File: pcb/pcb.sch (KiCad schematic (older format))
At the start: 20 parts, among them J1 BAT+, J2 BAT-, J3 Molex, SW1 Reset, SW2 Flash, U1 BOB-13263, U2 ESP-12F, U3 TP4056, U4 GY-521, U5 VREG

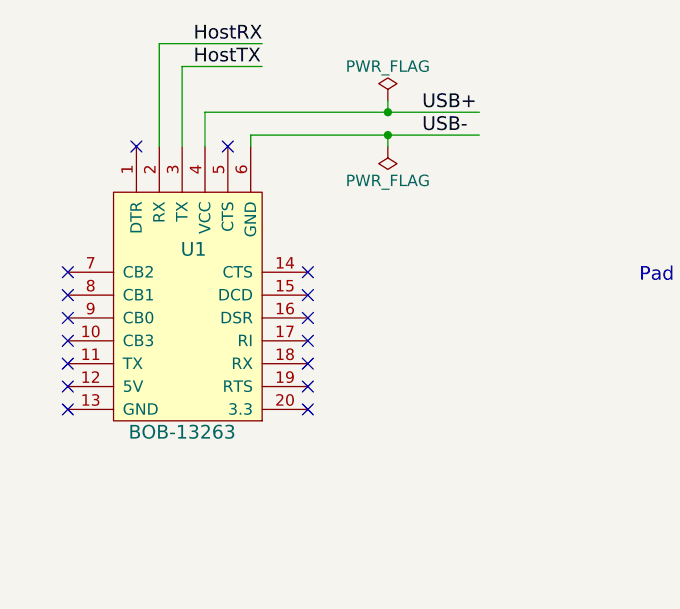
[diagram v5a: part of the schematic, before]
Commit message: PCB: use a smaller FTDI breakout board
The CP2102 USB Micro breakout boards look like they fit between the
pins of the TP4056 breakout board, which simplifies installation.
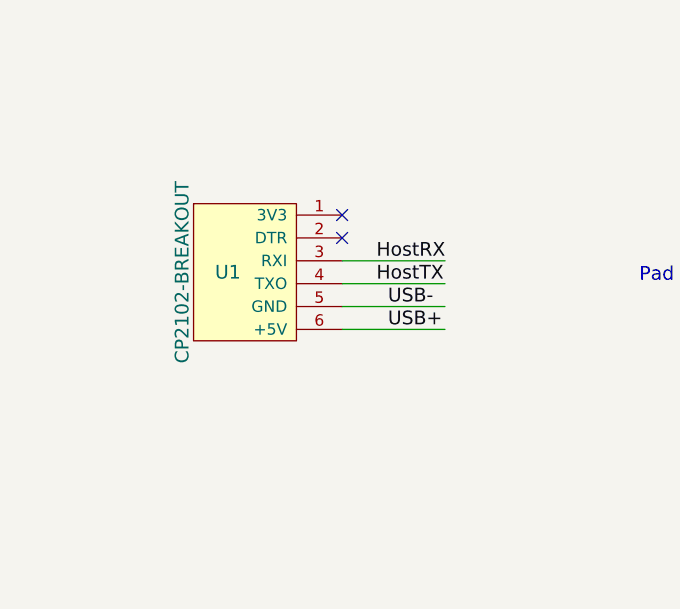
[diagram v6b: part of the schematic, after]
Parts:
- removed U1: BOB-13263, BOB13263:BOB-13263-TOP, symbol BOB-13263
- added U1: CP2102-BREAKOUT, CP2102-BRK:CP2102-BREAKOUT, symbol CP2102-BREAKOUT
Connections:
- wire segments 67 -> 61
- no-connect marks 28 -> 14
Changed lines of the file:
@@
 LIBS:tp4056
 LIBS:bob-13263
+LIBS:cp2102-breakout
 LIBS:pcb-cache
 EELAYER 25 0
@@
 $EndComp
 $Comp
-L PWR_FLAG #FLG01
-U 1 1 5B217D4E
-P 3800 1600
-F 0 "#FLG01" H 3800 1675 50  0001 C CNN
-F 1 "PWR_FLAG" H 3800 1750 50  0000 C CNN
-F 2 "" H 3800 1600 50  0001 C CNN
-F 3 "" H 3800 1600 50  0001 C CNN
-	1    3800 1600
-	1    0    0    -1
-$EndComp
-$Comp
-L PWR_FLAG #FLG02
-U 1 1 5B219669
-P 3800 1800
-F 0 "#FLG02" H 3800 1875 50  0001 C CNN
-F 1 "PWR_FLAG" H 3800 1950 50  0000 C CNN
-F 2 "" H 3800 1800 50  0001 C CNN
-F 3 "" H 3800 1800 50  0001 C CNN
-	1    3800 1800
-	-1   0    0    1
-$EndComp
-$Comp
 L SW_Push SW2
 U 1 1 5B21A301
@@
 	0    1    1    0
 $EndComp
-Text Label 3950 1650 0    60   ~ 0
+Text Label 3800 2600 0    60   ~ 0
 USB+
-Text Label 2950 1450 0    60   ~ 0
+Text Label 3750 2400 0    60   ~ 0
 HostTX
-Text Label 2950 1350 0    60   ~ 0
+Text Label 3750 2300 0    60   ~ 0
 HostRX
 Text Label 7300 2400 0    60   ~ 0
@@
 Text Label 5400 2150 1    60   ~ 0
 BAT+
-Text Label 3950 1750 0    60   ~ 0
+Text Label 3800 2500 0    60   ~ 0
 USB-
 Text Label 2300 5450 0    60   ~ 0
@@
 $EndComp
 $Comp
-L PWR_FLAG #FLG03
+L PWR_FLAG #FLG01
 U 1 1 5B22D046
 P 2850 5950
-F 0 "#FLG03" H 2850 6025 50  0001 C CNN
+F 0 "#FLG01" H 2850 6025 50  0001 C CNN
 F 1 "PWR_FLAG" H 2850 6100 50  0000 C CNN
 F 2 "" H 2850 5950 50  0001 C CNN
@@
 	-1   0    0    1
 $EndComp
-$Comp
-L BOB-13263 U1
-U 1 1 5B21DE34
-P 2600 2000
-F 0 "U1" H 2950 1750 60  0000 C CNN
-F 1 "BOB-13263" H 2900 950 60  0000 C CNN
-F 2 "BOB13263:BOB-13263-TOP" H 2600 2000 60  0001 C CNN
-F 3 "" H 2600 2000 60  0001 C CNN
-	1    2600 2000
-	1    0    0    -1
-$EndComp
-NoConn ~ 3100 1800
-NoConn ~ 2700 1800
-NoConn ~ 3450 2350
-NoConn ~ 3450 2450
-NoConn ~ 3450 2550
-NoConn ~ 3450 2650
-NoConn ~ 3450 2750
-NoConn ~ 3450 2850
-NoConn ~ 3450 2950
-NoConn ~ 2400 2950
-NoConn ~ 2400 2850
-NoConn ~ 2400 2750
-NoConn ~ 2400 2650
-NoConn ~ 2400 2550
-NoConn ~ 2400 2450
-NoConn ~ 2400 2350
-$Comp
-L PWR_FLAG #FLG04
+NoConn ~ 3600 2100
+NoConn ~ 3600 2200
+$Comp
+L PWR_FLAG #FLG02
 U 1 1 5B2225EE
 P 5700 3100
-F 0 "#FLG04" H 5700 3175 50  0001 C CNN
+F 0 "#FLG02" H 5700 3175 50  0001 C CNN
 F 1 "PWR_FLAG" H 5700 3250 50  0000 C CNN
 F 2 "" H 5700 3100 50  0001 C CNN
@@
 	-1   0    0    1
 $EndComp
-Wire Wire Line
-	3000 1650 4200 1650
-Wire Wire Line
-	3000 1650 3000 1800
-Connection ~ 3800 1650
-Wire Wire Line
-	7450 2400 7250 2400
-Wire Wire Line
-	7450 2500 7250 2500
-Wire Wire Line
-	5950 2850 5950 3050
-Wire Wire Line
-	5950 3050 5700 3050
-Wire Wire Line
-	5950 2150 5950 1950
-Wire Wire Line
-	5950 1950 6350 1950
-Wire Wire Line
-	8000 2250 8550 2250
-Wire Wire Line
-	8850 2550 8850 3000
-Wire Wire Line
-	9150 2250 10050 2250
-Wire Wire Line
-	5400 2250 5950 2250
-Wire Wire Line
-	5000 5500 5400 5500
-Wire Wire Line
-	5000 5600 5400 5600
-Wire Wire Line
-	5000 5700 5400 5700
-Wire Wire Line
-	5000 5800 5400 5800
-Wire Wire Line
-	2200 6200 3200 6200
-Wire Wire Line
-	5000 6200 6100 6200
-Wire Wire Line
-	7100 5500 7400 5500
-Wire Wire Line
-	7100 5600 7400 5600
-Wire Wire Line
-	7100 5700 7400 5700
-Wire Wire Line
-	7100 5800 7400 5800
-Wire Wire Line
-	7100 6100 7400 6100
-Wire Wire Line
-	6100 6000 5300 6000
-Wire Wire Line
-	3150 5150 3150 5500
-Wire Wire Line
-	2800 5300 3150 5300
-Wire Wire Line
-	2200 5300 2500 5300
-Wire Wire Line
-	3150 4750 3150 4600
-Connection ~ 3150 5300
-Wire Wire Line
-	2200 5700 2900 5700
-Wire Wire Line
-	2200 5300 2200 6200
-Connection ~ 2200 5300
-Wire Wire Line
-	2500 5900 3200 5900
-Wire Wire Line
-	5000 5900 5800 5900
-Wire Wire Line
-	5650 5100 5650 5900
-Connection ~ 5650 5900
-Wire Wire Line
-	5650 4600 5650 4700
-Wire Wire Line
-	3150 4600 5650 4600
-Wire Wire Line
-	4400 4600 4400 4350
-Connection ~ 4400 4600
-Connection ~ 2200 5700
-Wire Wire Line
-	6100 5600 6100 6000
-Connection ~ 6100 5900
-Wire Wire Line
-	5000 6100 5250 6100
-Wire Wire Line
-	5550 6100 5700 6100
-Wire Wire Line
-	3150 5500 3200 5500
-Wire Wire Line
-	2850 5950 2850 5900
-Connection ~ 2850 5900
-Wire Wire Line
-	5400 2250 5400 1950
-Connection ~ 5400 2250
-Wire Wire Line
-	3200 1800 3200 1750
-Wire Wire Line
-	3200 1750 4200 1750
-Wire Wire Line
-	3800 1600 3800 1650
-Wire Wire Line
-	3800 1800 3800 1750
-Connection ~ 3800 1750
-Wire Wire Line
-	2800 1800 2800 1350
-Wire Wire Line
-	2800 1350 3250 1350
-Wire Wire Line
-	2900 1450 2900 1800
-Wire Wire Line
-	2900 1450 3250 1450
-Wire Wire Line
-	5400 2550 5950 2550
-Wire Wire Line
-	5950 2550 5950 2750
-Wire Wire Line
-	5700 3050 5700 3100
-Wire Wire Line
-	5550 1850 5550 2250
-Connection ~ 5550 2250
-Wire Wire Line
-	5650 1850 5650 2550
-Connection ~ 5650 2550
-Wire Wire Line
-	2300 5450 2750 5450
-Wire Wire Line
-	3050 5450 3050 5600
-Wire Wire Line
-	2850 5600 3200 5600
-Connection ~ 3050 5600
-Wire Wire Line
-	2550 5600 2300 5600
-Wire Wire Line
-	3100 6200 3100 7000
-Wire Wire Line
-	3100 7000 3950 7000
-Connection ~ 3100 6200
-Wire Wire Line
-	5250 7000 4250 7000
-Wire Wire Line
-	9550 2700 9550 2550
-Wire Wire Line
-	8300 2700 9550 2700
-Connection ~ 9550 2250
-Connection ~ 8300 2250
-Wire Wire Line
-	8300 2550 8300 2700
-Wire Wire Line
-	5250 7000 5250 6200
-Connection ~ 5250 6200
-Wire Wire Line
-	5700 6100 5700 6200
-Connection ~ 5700 6200
-Connection ~ 8850 2700
 $Comp
 L C C1
@@
 	0    -1   -1   0
 $EndComp
+$Comp
+L CP2102-BREAKOUT U1
+U 1 1 5B258589
+P 2950 2050
+F 0 "U1" H 3100 1750 60  0000 C CNN
+F 1 "CP2102-BREAKOUT" V 2900 1750 60  0000 C CNN
+F 2 "CP2102-BRK:CP2102-BREAKOUT" H 2950 2050 60  0001 C CNN
+F 3 "" H 2950 2050 60  0001 C CNN
+	1    2950 2050
+	1    0    0    -1
+$EndComp
+Wire Wire Line
+	7450 2400 7250 2400
+Wire Wire Line
+	7450 2500 7250 2500
+Wire Wire Line
+	5950 2850 5950 3050
+Wire Wire Line
+	5950 3050 5700 3050
+Wire Wire Line
+	5950 2150 5950 1950
+Wire Wire Line
+	5950 1950 6350 1950
+Wire Wire Line
+	8000 2250 8550 2250
+Wire Wire Line
+	8850 2550 8850 3000
+Wire Wire Line
+	9150 2250 10050 2250
+Wire Wire Line
+	5400 2250 5950 2250
+Wire Wire Line
+	5000 5500 5400 5500
+Wire Wire Line
+	5000 5600 5400 5600
+Wire Wire Line
+	5000 5700 5400 5700
+Wire Wire Line
+	5000 5800 5400 5800
+Wire Wire Line
+	2200 6200 3200 6200
+Wire Wire Line
+	5000 6200 6100 6200
+Wire Wire Line
+	7100 5500 7400 5500
+Wire Wire Line
+	7100 5600 7400 5600
+Wire Wire Line
+	7100 5700 7400 5700
+Wire Wire Line
+	7100 5800 7400 5800
+Wire Wire Line
+	7100 6100 7400 6100
+Wire Wire Line
+	6100 6000 5300 6000
+Wire Wire Line
+	3150 5150 3150 5500
+Wire Wire Line
+	2800 5300 3150 5300
+Wire Wire Line
+	2200 5300 2500 5300
+Wire Wire Line
+	3150 4750 3150 4600
+Connection ~ 3150 5300
+Wire Wire Line
+	2200 5700 2900 5700
+Wire Wire Line
+	2200 5300 2200 6200
+Connection ~ 2200 5300
+Wire Wire Line
+	2500 5900 3200 5900
+Wire Wire Line
+	5000 5900 5800 5900
+Wire Wire Line
+	5650 5100 5650 5900
+Connection ~ 5650 5900
+Wire Wire Line
+	5650 4600 5650 4700
+Wire Wire Line
+	3150 4600 5650 4600
+Wire Wire Line
+	4400 4600 4400 4350
+Connection ~ 4400 4600
+Connection ~ 2200 5700
+Wire Wire Line
+	6100 5600 6100 6000
+Connection ~ 6100 5900
+Wire Wire Line
+	5000 6100 5250 6100
+Wire Wire Line
+	5550 6100 5700 6100
+Wire Wire Line
+	3150 5500 3200 5500
+Wire Wire Line
+	2850 5950 2850 5900
+Connection ~ 2850 5900
+Wire Wire Line
+	5400 2250 5400 1950
+Connection ~ 5400 2250
+Wire Wire Line
+	5400 2550 5950 2550
+Wire Wire Line
+	5950 2550 5950 2750
+Wire Wire Line
+	5700 3050 5700 3100
+Wire Wire Line
+	5550 1850 5550 2250
+Connection ~ 5550 2250
+Wire Wire Line
+	5650 1850 5650 2550
+Connection ~ 5650 2550
+Wire Wire Line
+	2300 5450 2750 5450
+Wire Wire Line
+	3050 5450 3050 5600
+Wire Wire Line
+	2850 5600 3200 5600
+Connection ~ 3050 5600
+Wire Wire Line
+	2550 5600 2300 5600
+Wire Wire Line
+	3100 6200 3100 7000
+Wire Wire Line
+	3100 7000 3950 7000
+Connection ~ 3100 6200
+Wire Wire Line
+	5250 7000 4250 7000
+Wire Wire Line
+	9550 2700 9550 2550
+Wire Wire Line
+	8300 2700 9550 2700
+Connection ~ 9550 2250
+Connection ~ 8300 2250
+Wire Wire Line
+	8300 2550 8300 2700
+Wire Wire Line
+	5250 7000 5250 6200
+Connection ~ 5250 6200
+Wire Wire Line
+	5700 6100 5700 6200
+Connection ~ 5700 6200
+Connection ~ 8850 2700
+Wire Wire Line
+	3600 2400 4050 2400
+Wire Wire Line
+	3600 2300 4050 2300
+Wire Wire Line
+	3600 2500 4050 2500
+Wire Wire Line
+	3600 2600 4050 2600
 $EndSCHEMATC

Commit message: Some more minor touch-ups
1. Remove silkscreen from pads which will take soldering
2. Fix some trace-via clearance issues (min 5 mil)
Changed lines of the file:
@@
 Title "Pendulum PCB"
 Date "2018-06-14"
-Rev "0.0.2"
+Rev "0.0.3"
 Comp ""
 Comment1 ""
@@
 Text Label 6100 5800 1    60   ~ 0
 3.3+
-Text Label 2250 5300 0    60   ~ 0
+Text Label 1900 5300 0    60   ~ 0
 3.3+
 Text Label 4400 4350 3    60   ~ 0
@@
 	2800 5300 3150 5300
 Wire Wire Line
-	2200 5300 2500 5300
+	1900 5300 2500 5300
 Wire Wire Line
 	3150 4750 3150 4600

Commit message: Some significant design changes
Thanks to u/Triabolical_ and u/alez from r/PrintedCircuitBoards for their
feedback and advice.

1. Switch to 805 resistors and the non-hand-soldered PCB pad footprints
They're not appreciably harder to solder, given that they're only 0.01"
smaller than the 1206 size, and they make routing considerably easier.
The non-hand-soldered size will be a bit trickier, but not all that
much trickier.

2. Move components around
The ESP-12 antenna performs much better when it's open to air on all
sides. It's now at the top of the board, poking off the edge. The switches
and pullup/downs now live right below the ESP-12, the GY521 pins go below
them, and everything else is mostly the same. The ESP-12 smoothing capacitor
now lives directly between the VCC and ground pins.

The overall package is now 0.2mm longer, but the routing is cleaner and
fewer vias are required.
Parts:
- C1, C2, C3: footprint Capacitors_SMD:C_1206_HandSoldering -> Capacitors_SMD:C_0805
- R1, R2, R3, R4, R5, R6, R7: footprint Resistors_SMD:R_1206_HandSoldering -> Resistors_SMD:R_0805
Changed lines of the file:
@@
 F 0 "R3" V 2980 5450 50  0000 C CNN
 F 1 "390k" V 2900 5450 50  0000 C CNN
-F 2 "Resistors_SMD:R_1206_HandSoldering" V 2830 5450 50  0001 C CNN
+F 2 "Resistors_SMD:R_0805" V 2830 5450 50  0001 C CNN
 F 3 "" H 2900 5450 50  0001 C CNN
 	1    2900 5450
@@
 F 0 "R1" V 2730 5300 50  0000 C CNN
 F 1 "10k" V 2650 5300 50  0000 C CNN
-F 2 "Resistors_SMD:R_1206_HandSoldering" V 2580 5300 50  0001 C CNN
+F 2 "Resistors_SMD:R_0805" V 2580 5300 50  0001 C CNN
 F 3 "" H 2650 5300 50  0001 C CNN
 	1    2650 5300
@@
 F 0 "R5" V 5230 6000 50  0000 C CNN
 F 1 "10k" V 5150 6000 50  0000 C CNN
-F 2 "Resistors_SMD:R_1206_HandSoldering" V 5080 6000 50  0001 C CNN
+F 2 "Resistors_SMD:R_0805" V 5080 6000 50  0001 C CNN
 F 3 "" H 5150 6000 50  0001 C CNN
 	1    5150 6000
@@
 F 0 "R4" V 3130 5700 50  0000 C CNN
 F 1 "10k" V 3050 5700 50  0000 C CNN
-F 2 "Resistors_SMD:R_1206_HandSoldering" V 2980 5700 50  0001 C CNN
+F 2 "Resistors_SMD:R_0805" V 2980 5700 50  0001 C CNN
 F 3 "" H 3050 5700 50  0001 C CNN
 	1    3050 5700
@@
 F 0 "R7" V 6030 5900 50  0000 C CNN
 F 1 "10k" V 5950 5900 50  0000 C CNN
-F 2 "Resistors_SMD:R_1206_HandSoldering" V 5880 5900 50  0001 C CNN
+F 2 "Resistors_SMD:R_0805" V 5880 5900 50  0001 C CNN
 F 3 "" H 5950 5900 50  0001 C CNN
 	1    5950 5900
@@
 F 0 "R6" V 5480 6100 50  0000 C CNN
 F 1 "10k" V 5400 6100 50  0000 C CNN
-F 2 "Resistors_SMD:R_1206_HandSoldering" V 5330 6100 50  0001 C CNN
+F 2 "Resistors_SMD:R_0805" V 5330 6100 50  0001 C CNN
 F 3 "" H 5400 6100 50  0001 C CNN
 	1    5400 6100
@@
 F 0 "C3" H 9575 2500 50  0000 L CNN
 F 1 "1uF" H 9575 2300 50  0000 L CNN
-F 2 "Capacitors_SMD:C_1206_HandSoldering" H 9588 2250 50  0001 C CNN
+F 2 "Capacitors_SMD:C_0805" H 9588 2250 50  0001 C CNN
 F 3 "" H 9550 2400 50  0001 C CNN
 	1    9550 2400
@@
 F 0 "R2" V 2780 5600 50  0000 C CNN
 F 1 "120k" V 2700 5600 50  0000 C CNN
-F 2 "Resistors_SMD:R_1206_HandSoldering" V 2630 5600 50  0001 C CNN
+F 2 "Resistors_SMD:R_0805" V 2630 5600 50  0001 C CNN
 F 3 "" H 2700 5600 50  0001 C CNN
 	1    2700 5600
@@
 F 0 "C2" H 8325 2500 50  0000 L CNN
 F 1 "1uF" H 8325 2300 50  0000 L CNN
-F 2 "Capacitors_SMD:C_1206_HandSoldering" H 8338 2250 50  0001 C CNN
+F 2 "Capacitors_SMD:C_0805" H 8338 2250 50  0001 C CNN
 F 3 "" H 8300 2400 50  0001 C CNN
 	1    8300 2400
@@
 F 0 "C1" H 4125 7100 50  0000 L CNN
 F 1 "47uF" H 4125 6900 50  0000 L CNN
-F 2 "Capacitors_SMD:C_1206_HandSoldering" H 4138 6850 50  0001 C CNN
+F 2 "Capacitors_SMD:C_0805" H 4138 6850 50  0001 C CNN
 F 3 "" H 4100 7000 50  0001 C CNN
 	1    4100 7000
